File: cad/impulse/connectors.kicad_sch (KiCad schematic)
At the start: 34 parts, among them J10 Conn_01x14_Socket, J11 DB125-2.54, J12 DB125-2.54, J2 DB125-2.54, J3 DB125-2.54, J4 Conn_01x06, J5 Conn_01x06, J6 Conn_01x06, J7 DB125-2.54, J8 GT-USB-7010ASV, J9 DB125-2.54, U4 LN2324DT2AG, U5 LN2324DT2AG, U6 USBLC6-2SC6, U7 LN2324DT2AG, U8 LN2324DT2AG

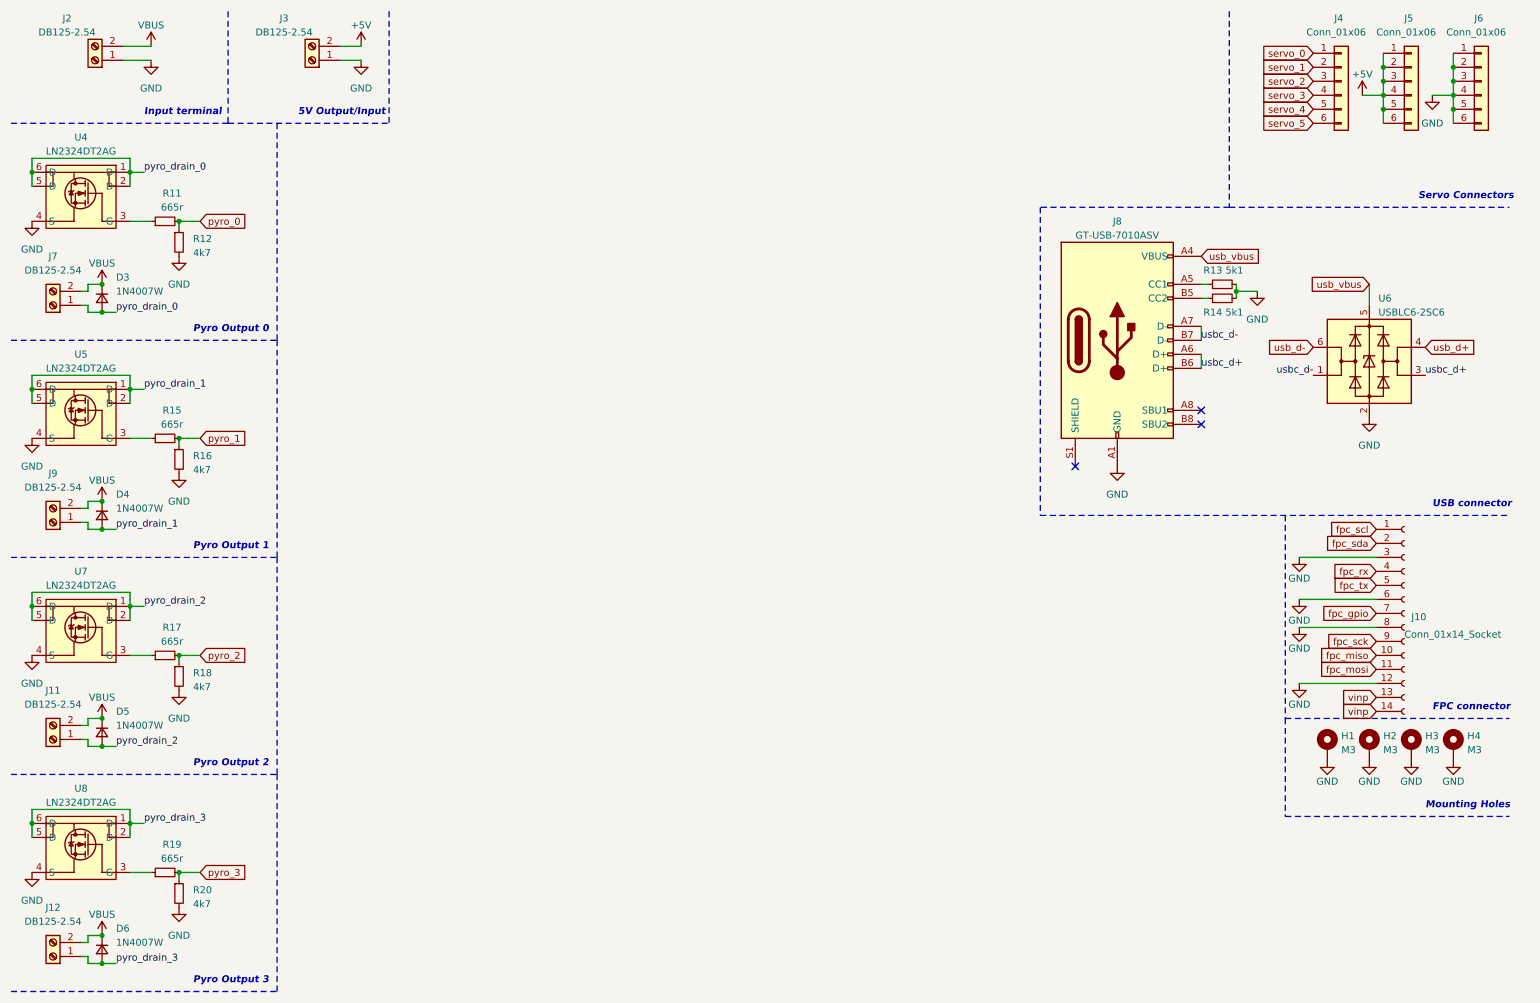
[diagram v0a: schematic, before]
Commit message: Modified oscillator circuit.
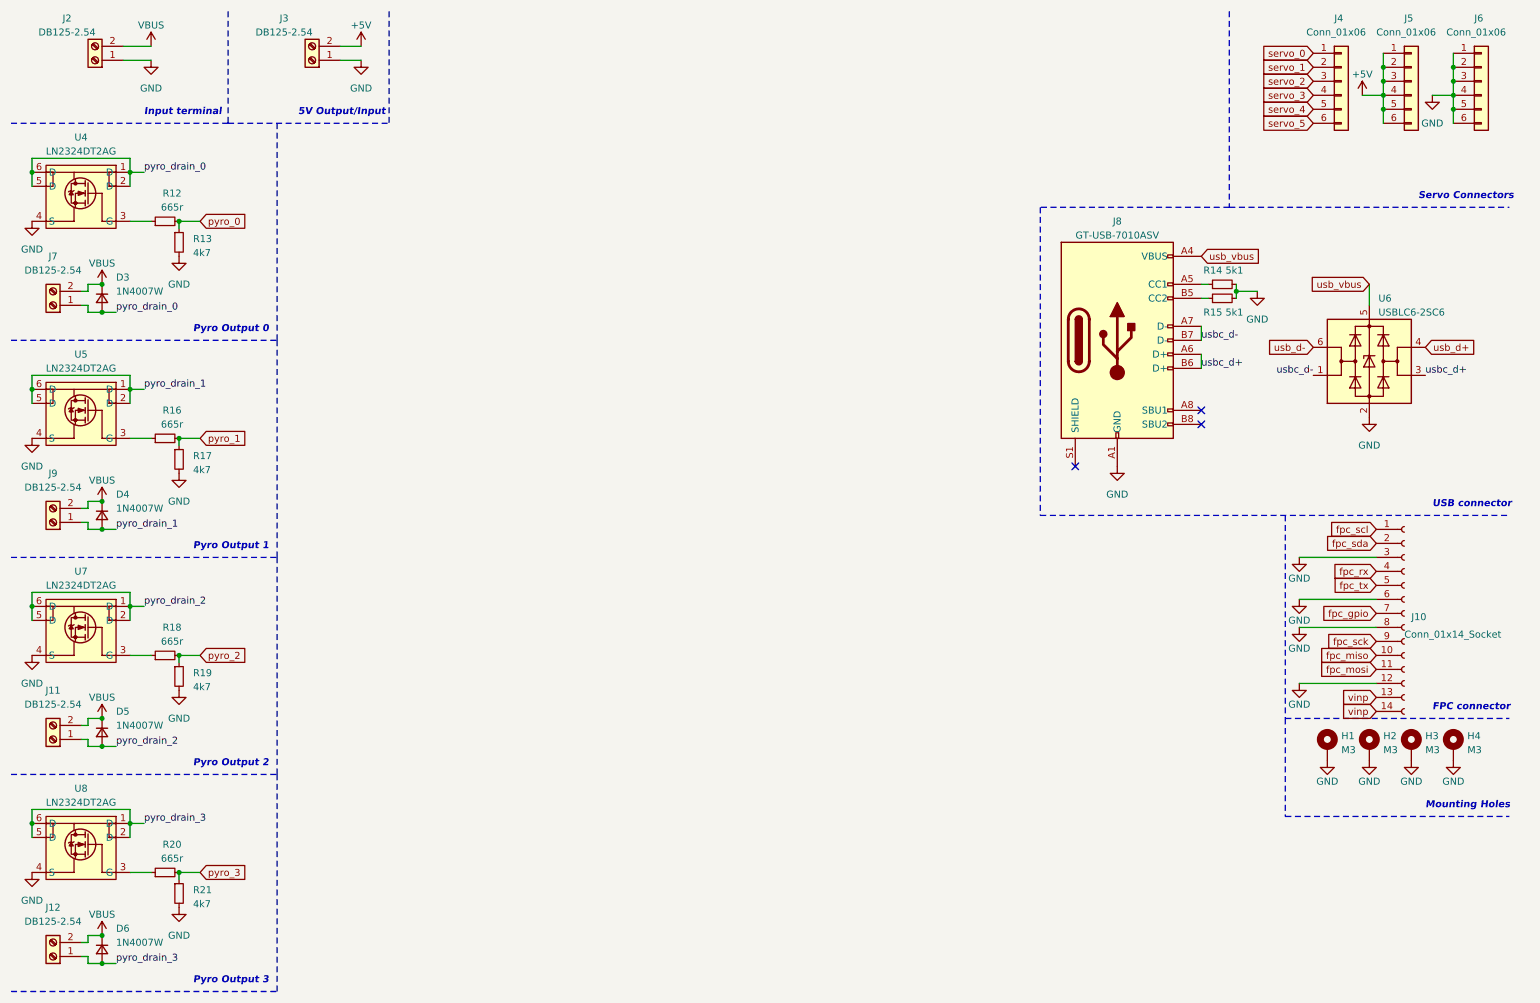
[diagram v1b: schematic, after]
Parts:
- renumbered R11 to R12, R12 to R13, R13 to R14, R14 to R15, R15 to R16, R16 to R17, R17 to R18, R18 to R19, R19 to R20, R20 to R21
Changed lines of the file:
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@@
   (symbol (lib_id "Device:R_Small") (at 232.41 64.77 90) (unit 1)
     (in_bom yes) (on_board yes) (dnp no)
-    (property "Reference" "R14" (at 232.41 67.31 90)
+    (property "Reference" "R15" (at 232.41 67.31 90)
       (effects (font (size 1.27 1.27)) (justify left))
     )
@@
       (project "impulse"
         (path "/eb4cfece-5fcb-437a-ac58-337ab6512039/bd071931-4d7b-4c0e-9292-4e2ffd2aeeb4"
-          (reference "R14") (unit 1)
+          (reference "R15") (unit 1)
         )
       )
@@
   (symbol (lib_id "Device:R_Small") (at 43.18 93.98 0) (unit 1)
     (in_bom yes) (on_board yes) (dnp no) (fields_autoplaced)
-    (property "Reference" "R16" (at 45.72 93.345 0)
+    (property "Reference" "R17" (at 45.72 93.345 0)
       (effects (font (size 1.27 1.27)) (justify left))
     )
@@
       (project "impulse"
         (path "/eb4cfece-5fcb-437a-ac58-337ab6512039/bd071931-4d7b-4c0e-9292-4e2ffd2aeeb4"
-          (reference "R16") (unit 1)
+          (reference "R17") (unit 1)
         )
       )
@@
   (symbol (lib_id "Device:R_Small") (at 43.18 133.35 0) (unit 1)
     (in_bom yes) (on_board yes) (dnp no) (fields_autoplaced)
-    (property "Reference" "R18" (at 45.72 132.715 0)
+    (property "Reference" "R19" (at 45.72 132.715 0)
       (effects (font (size 1.27 1.27)) (justify left))
     )
@@
       (project "impulse"
         (path "/eb4cfece-5fcb-437a-ac58-337ab6512039/bd071931-4d7b-4c0e-9292-4e2ffd2aeeb4"
-          (reference "R18") (unit 1)
+          (reference "R19") (unit 1)
         )
       )
@@
   (symbol (lib_id "Device:R_Small") (at 232.41 62.23 90) (unit 1)
     (in_bom yes) (on_board yes) (dnp no)
-    (property "Reference" "R13" (at 232.41 59.69 90)
+    (property "Reference" "R14" (at 232.41 59.69 90)
       (effects (font (size 1.27 1.27)) (justify left))
     )
@@
       (project "impulse"
         (path "/eb4cfece-5fcb-437a-ac58-337ab6512039/bd071931-4d7b-4c0e-9292-4e2ffd2aeeb4"
-          (reference "R13") (unit 1)
+          (reference "R14") (unit 1)
         )
       )
@@
   (symbol (lib_id "Device:R_Small") (at 40.64 50.8 90) (unit 1)
     (in_bom yes) (on_board yes) (dnp no)
-    (property "Reference" "R11" (at 41.91 45.72 90)
+    (property "Reference" "R12" (at 41.91 45.72 90)
       (effects (font (size 1.27 1.27)))
     )
@@
       (project "impulse"
         (path "/eb4cfece-5fcb-437a-ac58-337ab6512039/bd071931-4d7b-4c0e-9292-4e2ffd2aeeb4"
-          (reference "R11") (unit 1)
+          (reference "R12") (unit 1)
         )
       )
@@
   (symbol (lib_id "Device:R_Small") (at 40.64 129.54 90) (unit 1)
     (in_bom yes) (on_board yes) (dnp no)
-    (property "Reference" "R17" (at 41.91 124.46 90)
+    (property "Reference" "R18" (at 41.91 124.46 90)
       (effects (font (size 1.27 1.27)))
     )
@@
       (project "impulse"
         (path "/eb4cfece-5fcb-437a-ac58-337ab6512039/bd071931-4d7b-4c0e-9292-4e2ffd2aeeb4"
-          (reference "R17") (unit 1)
+          (reference "R18") (unit 1)
         )
       )
@@
   (symbol (lib_id "Device:R_Small") (at 40.64 168.91 90) (unit 1)
     (in_bom yes) (on_board yes) (dnp no)
-    (property "Reference" "R19" (at 41.91 163.83 90)
+    (property "Reference" "R20" (at 41.91 163.83 90)
       (effects (font (size 1.27 1.27)))
     )
@@
       (project "impulse"
         (path "/eb4cfece-5fcb-437a-ac58-337ab6512039/bd071931-4d7b-4c0e-9292-4e2ffd2aeeb4"
-          (reference "R19") (unit 1)
+          (reference "R20") (unit 1)
         )
       )
@@
   (symbol (lib_id "Device:R_Small") (at 43.18 172.72 0) (unit 1)
     (in_bom yes) (on_board yes) (dnp no) (fields_autoplaced)
-    (property "Reference" "R20" (at 45.72 172.085 0)
+    (property "Reference" "R21" (at 45.72 172.085 0)
       (effects (font (size 1.27 1.27)) (justify left))
     )
@@
       (project "impulse"
         (path "/eb4cfece-5fcb-437a-ac58-337ab6512039/bd071931-4d7b-4c0e-9292-4e2ffd2aeeb4"
-          (reference "R20") (unit 1)
+          (reference "R21") (unit 1)
         )
       )
@@
   (symbol (lib_id "Device:R_Small") (at 40.64 90.17 90) (unit 1)
     (in_bom yes) (on_board yes) (dnp no)
-    (property "Reference" "R15" (at 41.91 85.09 90)
+    (property "Reference" "R16" (at 41.91 85.09 90)
       (effects (font (size 1.27 1.27)))
     )
@@
       (project "impulse"
         (path "/eb4cfece-5fcb-437a-ac58-337ab6512039/bd071931-4d7b-4c0e-9292-4e2ffd2aeeb4"
-          (reference "R15") (unit 1)
+          (reference "R16") (unit 1)
         )
       )
@@
   (symbol (lib_id "Device:R_Small") (at 43.18 54.61 0) (unit 1)
     (in_bom yes) (on_board yes) (dnp no) (fields_autoplaced)
-    (property "Reference" "R12" (at 45.72 53.975 0)
+    (property "Reference" "R13" (at 45.72 53.975 0)
       (effects (font (size 1.27 1.27)) (justify left))
     )
@@
       (project "impulse"
         (path "/eb4cfece-5fcb-437a-ac58-337ab6512039/bd071931-4d7b-4c0e-9292-4e2ffd2aeeb4"
-          (reference "R12") (unit 1)
-        )
-      )
+          (reference "R13") (unit 1)
+        )
+      )

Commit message: First layout.
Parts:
- removed J3: DB125-2.54, TerminalBlock_TE-Connectivity:TerminalBlock_TE_282834-2_1x02_P2.54mm_Horizontal, symbol Connector:Screw_Terminal_01x02
- added R25, R26: 1k5, Resistor_SMD:R_0402_1005Metric, symbol Device:R_Small
- renumbered R12 to R13, R13 to R14, R14 to R15, R15 to R16, R16 to R17, R17 to R18, R18 to R19, R19 to R20, R20 to R21, R21 to R22
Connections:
- net fpc_scl: now also R25.2
- net fpc_sda: now also R26.2
- new net +3V3: R25.1, R26.1
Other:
- note removed: "5V Output/Input"

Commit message: Final version, ordered it.
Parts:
- D3, D4, D5, D6: lcsc C2944153 -> C727082
- U4, U5, U7, U8: value LN2324DT2AG -> G2014; lcsc C172432 -> C3038579
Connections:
- net servo_0: now also J4.3 (Pin_3); no longer J4.1 (Pin_1)
- net servo_2: now also J4.4 (Pin_4); no longer J4.3 (Pin_3)
- net servo_3: now also J4.1 (Pin_1); no longer J4.4 (Pin_4)
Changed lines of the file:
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@@
+    (stroke (width 0) (type default))
+  )
+  (wire (pts (xy 242.57 25.4) (xy 248.92 25.4))
     (stroke (width 0) (type default))
   )
@@
     (stroke (width 0) (type default))
   )
+  (wire (pts (xy 242.57 20.32) (xy 248.92 20.32))
+    (stroke (width 0) (type default))
+  )
   (wire (pts (xy 29.21 106.68) (xy 31.75 106.68))
-    (stroke (width 0) (type default))
-  )
-  (wire (pts (xy 242.57 22.86) (xy 248.92 22.86))
     (stroke (width 0) (type default))
   )
@@
     (stroke (width 0) (type dash))
   )
+  (wire (pts (xy 242.57 22.86) (xy 248.92 22.86))
+    (stroke (width 0) (type default))
+  )
   (wire (pts (xy 25.4 181.61) (xy 26.67 181.61))
     (stroke (width 0) (type default))
@@
     (stroke (width 0) (type default))
   )
+  (wire (pts (xy 242.57 27.94) (xy 248.92 27.94))
+    (stroke (width 0) (type default))
+  )
   (wire (pts (xy 16.51 39.37) (xy 34.29 39.37))
     (stroke (width 0) (type default))
@@
     (stroke (width 0) (type dash))
   )
-  (wire (pts (xy 242.57 20.32) (xy 248.92 20.32))
-    (stroke (width 0) (type default))
-  )
   (wire (pts (xy 16.51 120.65) (xy 16.51 118.11))
     (stroke (width 0) (type default))
@@
     (stroke (width 0) (type default))
   )
-  (wire (pts (xy 242.57 27.94) (xy 248.92 27.94))
-    (stroke (width 0) (type default))
-  )
   (wire (pts (xy 267.97 115.57) (xy 267.97 120.65))
     (stroke (width 0) (type default))
@@
   )
   (wire (pts (xy 25.4 102.87) (xy 26.67 102.87))
-    (stroke (width 0) (type default))
-  )
-  (wire (pts (xy 242.57 25.4) (xy 248.92 25.4))
     (stroke (width 0) (type default))
   )
@@
     )
   )
-  (global_label "servo_0" (shape input) (at 242.57 20.32 180) (fields_autoplaced)
+  (global_label "servo_0" (shape input) (at 242.57 25.4 180) (fields_autoplaced)
+    (effects (font (size 1.27 1.27)) (justify right))
+    (property "Intersheetrefs" "${INTERSHEET_REFS}" (at 232.4676 25.4 0)
+      (effects (font (size 1.27 1.27)) (justify right) hide)
+    )
+  )
+  (global_label "servo_3" (shape input) (at 242.57 20.32 180) (fields_autoplaced)
     (effects (font (size 1.27 1.27)) (justify right))
     (property "Intersheetrefs" "${INTERSHEET_REFS}" (at 232.4676 20.32 0)
-      (effects (font (size 1.27 1.27)) (justify right) hide)
-    )
-  )
-  (global_label "servo_3" (shape input) (at 242.57 27.94 180) (fields_autoplaced)
-    (effects (font (size 1.27 1.27)) (justify right))
-    (property "Intersheetrefs" "${INTERSHEET_REFS}" (at 232.4676 27.94 0)
       (effects (font (size 1.27 1.27)) (justify right) hide)
     )
@@
     )
   )
-  (global_label "servo_2" (shape input) (at 242.57 25.4 180) (fields_autoplaced)
+  (global_label "servo_2" (shape input) (at 242.57 27.94 180) (fields_autoplaced)
     (effects (font (size 1.27 1.27)) (justify right))
-    (property "Intersheetrefs" "${INTERSHEET_REFS}" (at 232.4676 25.4 0)
+    (property "Intersheetrefs" "${INTERSHEET_REFS}" (at 232.4676 27.94 0)
       (effects (font (size 1.27 1.27)) (justify right) hide)
     )
@@
       (effects (font (size 1.27 1.27)) hide)
     )
-    (property "lcsc" "C2944153" (at 29.21 143.51 0)
+    (property "lcsc" "C727082" (at 29.21 143.51 0)
       (effects (font (size 1.27 1.27)) hide)
     )
@@
       (effects (font (size 1.27 1.27)) hide)
     )
-    (property "lcsc" "C2944153" (at 29.21 104.14 0)
+    (property "lcsc" "C727082" (at 29.21 104.14 0)
       (effects (font (size 1.27 1.27)) hide)
     )
@@
       (effects (font (size 1.27 1.27)) hide)
     )
-    (property "lcsc" "C2944153" (at 29.21 64.77 0)
+    (property "lcsc" "C727082" (at 29.21 64.77 0)
       (effects (font (size 1.27 1.27)) hide)
     )
@@
       (effects (font (size 1.27 1.27)))
     )
-    (property "Value" "LN2324DT2AG" (at 25.4 156.21 0)
+    (property "Value" "G2014" (at 25.4 156.21 0)
       (effects (font (size 1.27 1.27)))
     )
@@
       (effects (font (size 1.27 1.27)) hide)
     )
-    (property "lcsc" " C172432" (at 25.4 151.13 0)
+    (property "lcsc" "C3038579" (at 25.4 151.13 0)
       (effects (font (size 1.27 1.27)) hide)
     )
@@
       (effects (font (size 1.27 1.27)) hide)
     )
-    (property "lcsc" "C2944153" (at 29.21 182.88 0)
+    (property "lcsc" "C727082" (at 29.21 182.88 0)
       (effects (font (size 1.27 1.27)) hide)
     )
@@
       (effects (font (size 1.27 1.27)))
     )
-    (property "Value" "LN2324DT2AG" (at 25.4 77.47 0)
+    (property "Value" "G2014" (at 25.4 77.47 0)
       (effects (font (size 1.27 1.27)))
     )
@@
       (effects (font (size 1.27 1.27)) hide)
     )
-    (property "lcsc" " C172432" (at 25.4 72.39 0)
+    (property "lcsc" "C3038579" (at 25.4 72.39 0)
       (effects (font (size 1.27 1.27)) hide)
     )
@@
       (effects (font (size 1.27 1.27)))
     )
-    (property "Value" "LN2324DT2AG" (at 25.4 116.84 0)
+    (property "Value" "G2014" (at 25.4 116.84 0)
       (effects (font (size 1.27 1.27)))
     )
@@
       (effects (font (size 1.27 1.27)) hide)
     )
-    (property "lcsc" " C172432" (at 25.4 111.76 0)
+    (property "lcsc" "C3038579" (at 25.4 111.76 0)
       (effects (font (size 1.27 1.27)) hide)
     )
@@
       (effects (font (size 1.27 1.27)))
     )
-    (property "Value" "LN2324DT2AG" (at 25.4 38.1 0)
+    (property "Value" "G2014" (at 25.4 38.1 0)
       (effects (font (size 1.27 1.27)))
     )
@@
       (effects (font (size 1.27 1.27)) hide)
     )
-    (property "lcsc" " C172432" (at 25.4 33.02 0)
-      (effects (font (size 1.27 1.27)) hide)
-    )
+    (property "lcsc" "C3038579" (at 25.4 33.02 0)
+      (effects (font (size 1.27 1.27)) hide)
+    )
